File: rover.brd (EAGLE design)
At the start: 73.7 x 53.3 mm, 16 parts, among them IC1 MC33269ST-5.0T3, J1 B02B-PASK(LF)(SN)

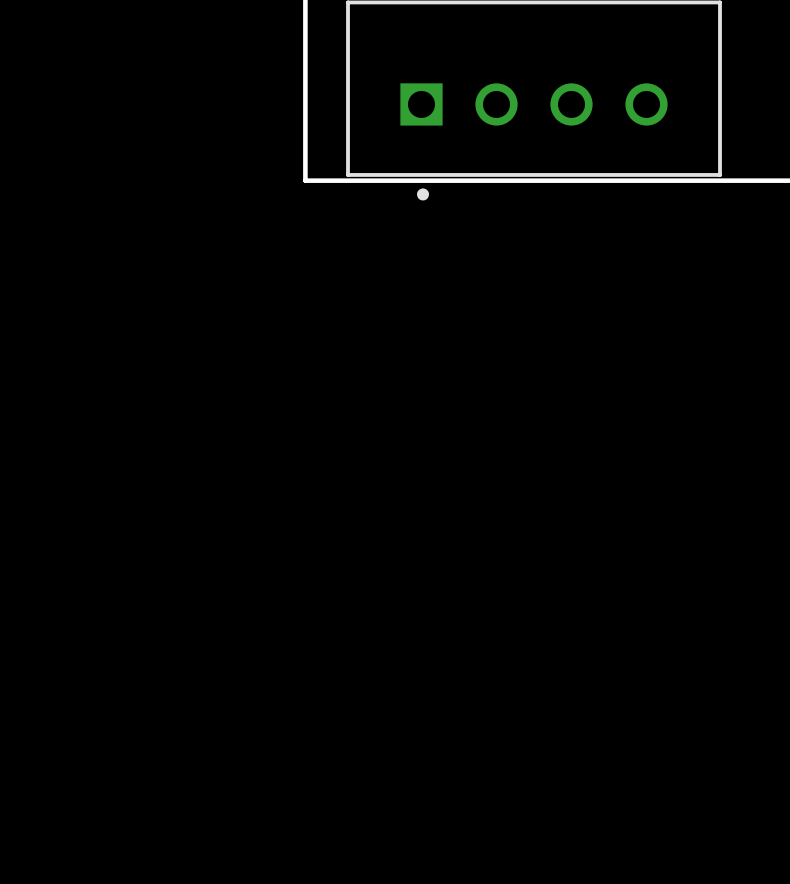
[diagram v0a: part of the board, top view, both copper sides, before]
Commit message: added esc and servo headers
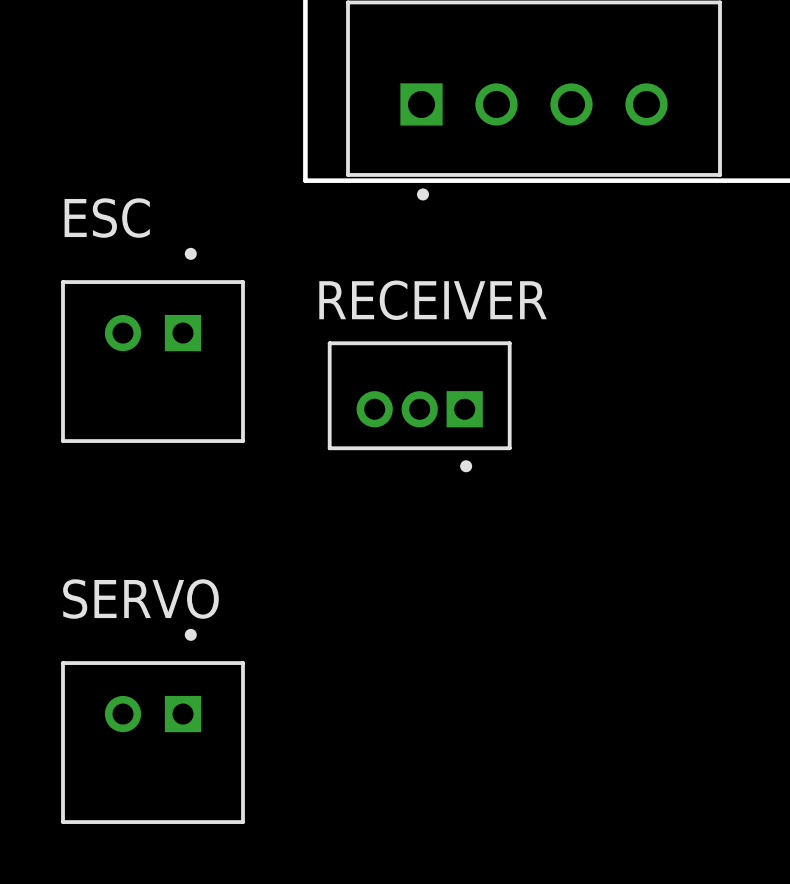
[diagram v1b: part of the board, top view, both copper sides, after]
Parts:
- added ESC, SERVO: B02B-PASK(LF)(SN), Headers:B02B-PASK(LF)(SN)
- added RECEIVER: B3B-ZR(LF)(SN), Headers:B3B-ZR(LF)(SN)
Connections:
- net ESC: now also ESC.1
- net GND: now also ESC.2, RECEIVER.3, SERVO.2
- net REC_ESC: now also RECEIVER.1
- net REC_SERVO: now also RECEIVER.2
- net SERVO: now also SERVO.1
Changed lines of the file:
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@@
 <drawing>
 <settings>
-<setting alwaysvectorfont="yes"/>
+<setting alwaysvectorfont="no"/>
 <setting verticaltext="up"/>
 </settings>
@@
 </element>
 <element name="U$5" library="Teensy-4.0" package="TEENSY_4.0-BASIC" value="TEENSY_4.0-BASIC" x="76.2" y="6.35" smashed="yes" rot="R180"/>
+<element name="RECEIVER" library="Headers" library_urn="urn:adsk.eagle:library:11687645" package="B3B-ZR(LF)(SN)" package3d_urn="urn:adsk.eagle:package:19181366/2" value="B3B-ZR(LF)(SN)" x="24.13" y="-10.16" smashed="yes">
+<attribute name="CREATED_BY" value="PCBLayout.com" x="15.24" y="0" size="1.778" layer="27" display="off"/>
+<attribute name="DIGIKEY_PARTNO" value="455-1658-ND" x="15.24" y="0" size="1.778" layer="27" display="off"/>
+<attribute name="MANUFACTURER" value="JST Sales America Inc." x="15.24" y="0" size="1.778" layer="27" display="off"/>
+<attribute name="MPN" value="B3B-ZR(LF)(SN)" x="15.24" y="0" size="1.778" layer="27" display="off"/>
+<attribute name="NAME" x="20.63" y="-7.16" size="1.27" layer="25"/>
+<attribute name="VALUE" x="20.63" y="-13.66" size="1.27" layer="27"/>
+</element>
+<element name="ESC" library="Headers" library_urn="urn:adsk.eagle:library:11687645" package="B02B-PASK(LF)(SN)" package3d_urn="urn:adsk.eagle:package:19181365/13" value="B02B-PASK(LF)(SN)" x="15.24" y="-7.62" smashed="yes">
+<attribute name="CREATED_BY" value="PCBLayout.com" x="15.24" y="-7.62" size="1.778" layer="27" display="off"/>
+<attribute name="DIGIKEY_PARTNO" value="455-1817-ND" x="15.24" y="-7.62" size="1.778" layer="27" display="off"/>
+<attribute name="MANUFACTURER" value="JST Sales America Inc." x="15.24" y="-7.62" size="1.778" layer="27" display="off"/>
+<attribute name="MPN" value="B02B-PASK(LF)(SN)" x="15.24" y="-7.62" size="1.778" layer="27" display="off"/>
+<attribute name="NAME" x="12.14" y="-4.42" size="1.27" layer="25"/>
+<attribute name="VALUE" x="11.84" y="-13.22" size="1.27" layer="27"/>
+</element>
+<element name="SERVO" library="Headers" library_urn="urn:adsk.eagle:library:11687645" package="B02B-PASK(LF)(SN)" package3d_urn="urn:adsk.eagle:package:19181365/13" value="B02B-PASK(LF)(SN)" x="15.24" y="-20.32" smashed="yes">
+<attribute name="CREATED_BY" value="PCBLayout.com" x="6.35" y="-7.62" size="1.778" layer="27" display="off"/>
+<attribute name="DIGIKEY_PARTNO" value="455-1817-ND" x="6.35" y="-7.62" size="1.778" layer="27" display="off"/>
+<attribute name="MANUFACTURER" value="JST Sales America Inc." x="6.35" y="-7.62" size="1.778" layer="27" display="off"/>
+<attribute name="MPN" value="B02B-PASK(LF)(SN)" x="6.35" y="-7.62" size="1.778" layer="27" display="off"/>
+<attribute name="NAME" x="12.14" y="-17.12" size="1.27" layer="25"/>
+<attribute name="VALUE" x="11.84" y="-25.92" size="1.27" layer="27"/>
+</element>
 </elements>
 <signals>
@@
 <contactref element="U$5" pad="GND2"/>
 <contactref element="GREEN" pad="C"/>
+<contactref element="RECEIVER" pad="3"/>
+<contactref element="ESC" pad="2"/>
+<contactref element="SERVO" pad="2"/>
 <wire x1="92.71" y1="13.97" x2="79.375" y2="29.21" width="0" layer="19" extent="1-1"/>
 <wire x1="90.17" y1="-1.27" x2="92.71" y2="13.97" width="0" layer="19" extent="1-1"/>
@@
 <wire x1="29.19" y1="11.43" x2="40.41" y2="21.59" width="0" layer="19" extent="1-1"/>
 <wire x1="29.19" y1="0" x2="29.19" y2="11.43" width="0" layer="19" extent="1-1"/>
+<wire x1="22.63" y1="-10.16" x2="29.19" y2="0" width="0" layer="19" extent="1-1"/>
+<wire x1="14.24" y1="-7.62" x2="22.63" y2="-10.16" width="0" layer="19" extent="1-1"/>
+<wire x1="14.24" y1="-20.32" x2="14.24" y2="-7.62" width="0" layer="19" extent="1-1"/>
 </signal>
 <signal name="SDA_5V">
@@
 <signal name="SERVO">
 <contactref element="U$5" pad="2"/>
+<contactref element="SERVO" pad="1"/>
+<wire x1="16.24" y1="-20.32" x2="85.09" y2="13.97" width="0" layer="19" extent="1-1"/>
 </signal>
 <signal name="ESC">
 <contactref element="U$5" pad="3/CANTX"/>
+<contactref element="ESC" pad="1"/>
+<wire x1="16.24" y1="-7.62" x2="82.55" y2="13.97" width="0" layer="19" extent="1-1"/>
 </signal>
 <signal name="RR_ENC_B">
@@
 <signal name="REC_SERVO">
 <contactref element="U$5" pad="14/A0"/>
+<contactref element="RECEIVER" pad="2"/>
+<wire x1="24.13" y1="-10.16" x2="62.23" y2="-1.27" width="0" layer="19" extent="1-1"/>
 </signal>
 <signal name="REC_ESC">
 <contactref element="U$5" pad="15/A1"/>
+<contactref element="RECEIVER" pad="1"/>
+<wire x1="25.63" y1="-10.16" x2="64.77" y2="-1.27" width="0" layer="19" extent="1-1"/>
 </signal>
 <signal name="+5V">

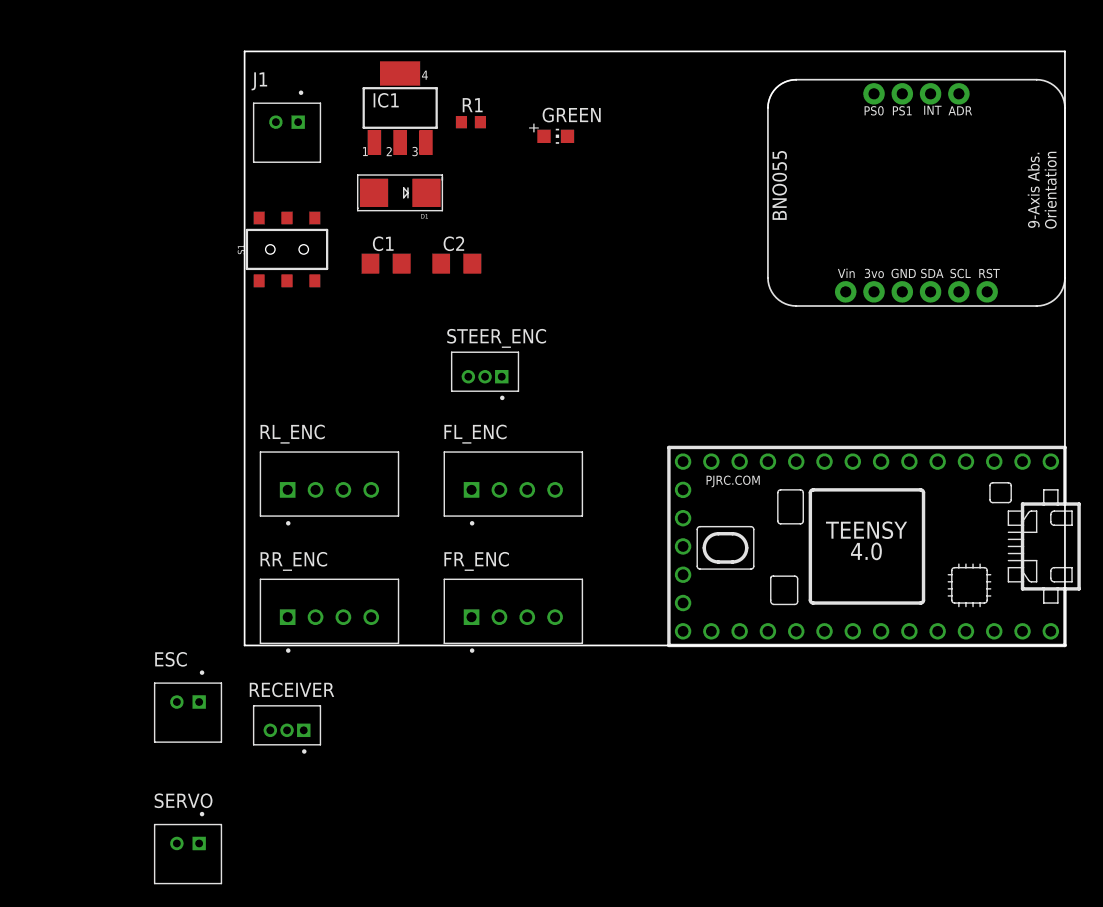
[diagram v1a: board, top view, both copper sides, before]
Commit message: added ground planes
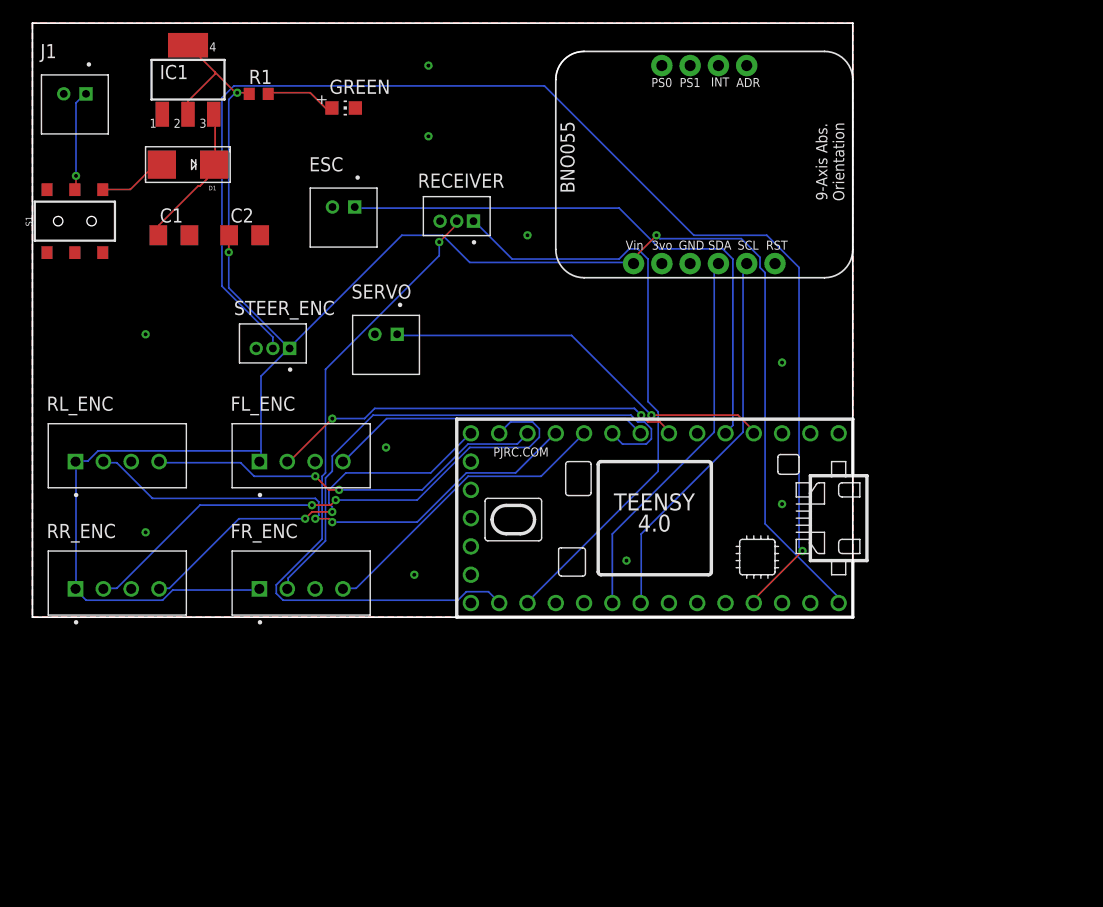
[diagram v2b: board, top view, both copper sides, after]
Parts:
- moved SERVO 49.1 mm to (33.0, 25.4)
- moved RECEIVER 48.2 mm to (39.4, 35.6)
- moved ESC 46.6 mm to (29.2, 36.8)
- moved FL_ENC 19.2 mm to (25.4, 14.0)
- moved U$5 19.2 mm to (57.1, 8.89)
- moved C1 19.2 mm to (14.0, 34.3)
- moved FR_ENC 19.2 mm to (25.4, 2.54)
- moved RL_ENC 19.2 mm to (8.89, 14.0)
- moved R1 19.2 mm to (21.6, 47.0)
- moved RR_ENC 19.2 mm to (8.89, 2.54)
- moved C2 19.2 mm to (20.3, 34.3)
- moved D1 19.2 mm to (15.2, 40.6)
- moved GREEN 19.2 mm to (29.2, 45.7)
- moved IC1 19.2 mm to (15.2, 48.3)
- moved J1 19.2 mm to (5.08, 47.0)
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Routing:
- net +5V: track 0.00 -> 180.3 mm, vias 0 -> 3
- net STEER_ENC: track 0.00 -> 115.5 mm, vias 0 -> 1
- net REC_SERVO: track 0.00 -> 61.2 mm, vias 0 -> 1
- net REC_ESC: track 0.00 -> 54.0 mm
- net ESC: track 0.00 -> 51.8 mm
- net RR_ENC_A: track 0.00 -> 49.8 mm, vias 0 -> 2
- net FR_ENC_A: track 0.00 -> 49.3 mm
- net RL_ENC_A: track 0.00 -> 47.5 mm, vias 0 -> 2
- net FL_ENC_A: track 0.00 -> 37.4 mm, vias 0 -> 2
- net RL_ENC_B: track 0.00 -> 36.3 mm, vias 0 -> 2
- net SERVO: track 0.00 -> 35.9 mm, vias 0 -> 1
- net RR_ENC_B: track 0.00 -> 35.4 mm, vias 0 -> 2
- net SDA_5V: track 0.00 -> 34.4 mm
- net SCL_5V: track 0.00 -> 34.4 mm
- net FL_ENC_B: track 0.00 -> 28.9 mm
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- added copper zone on layer 1, net GND
- added copper zone on layer 16, net GND
